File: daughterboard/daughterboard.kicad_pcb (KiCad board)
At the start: 2 copper layers, 85 x 56 mm, 1 part, among them P1 CONN_13X2

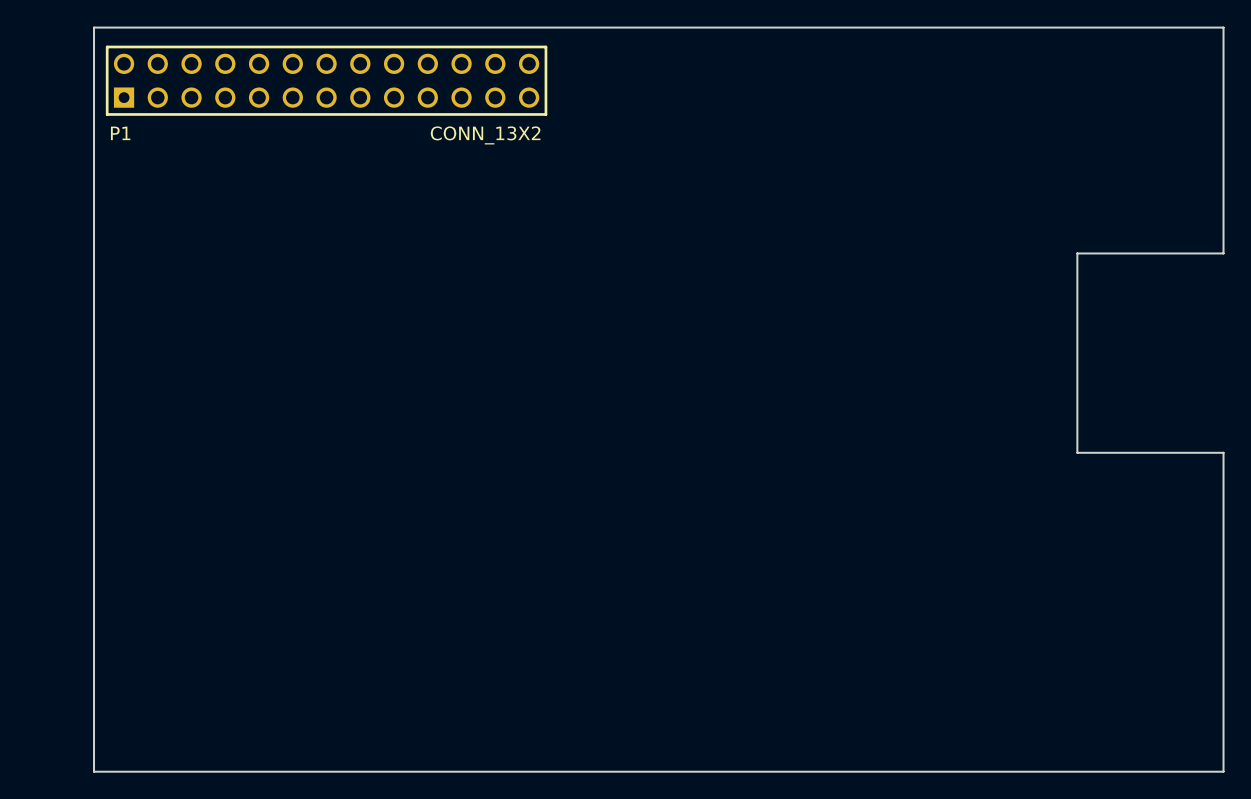
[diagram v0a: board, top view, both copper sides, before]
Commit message: Layout parts (backwards)
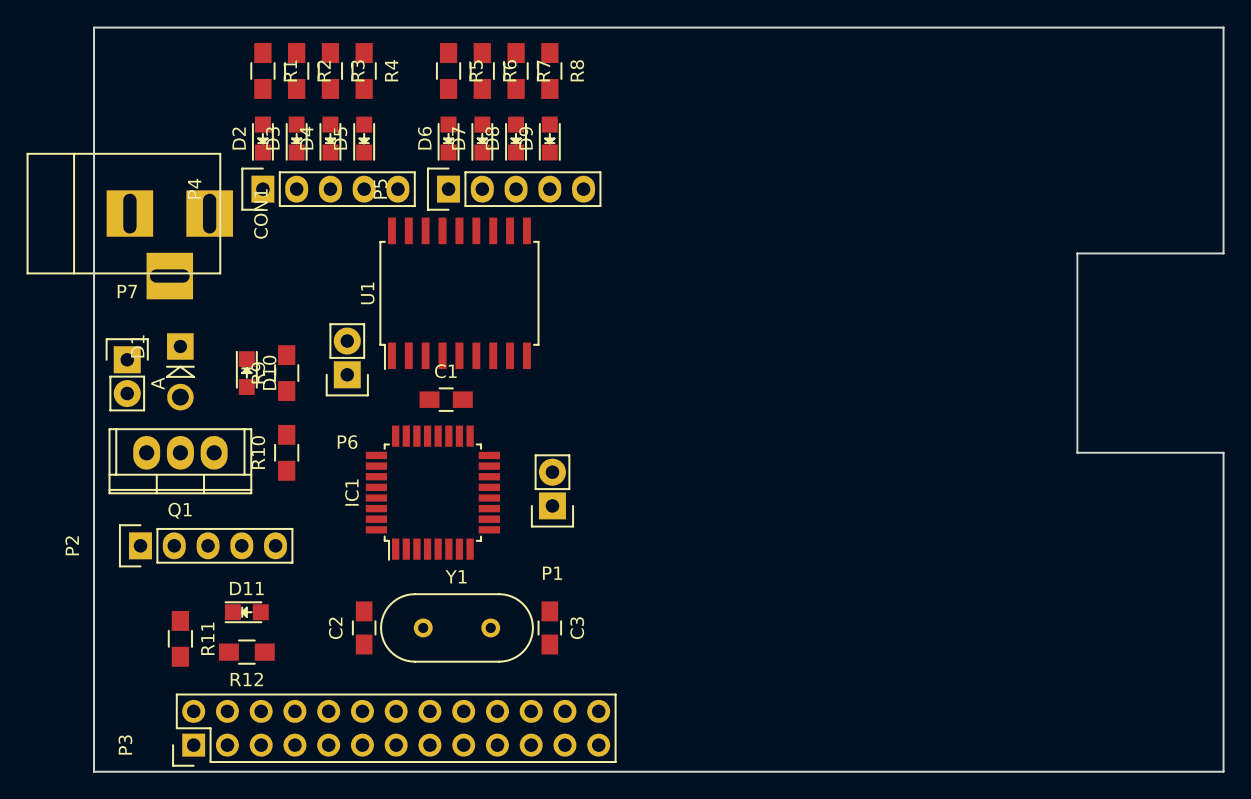
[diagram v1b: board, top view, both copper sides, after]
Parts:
- added C1: 100nF, Capacitors_SMD:C_0805_HandSoldering, F.Cu at (170.0, 153.0)
- added C2: 22pF, Capacitors_SMD:C_0805_HandSoldering, F.Cu at (163.8, 170.2)
- added C3: 22pF, Capacitors_SMD:C_0805_HandSoldering, F.Cu at (177.8, 170.2)
- added CON1: 12V_JACK, Connect:BARREL_JACK, F.Cu at (146.0, 139.0)
- added D1: 1N4007, Diodes_ThroughHole:Diode_DO-41_SOD81_Vertical_AnodeUp, F.Cu at (150.0, 149.0)
- added D10: YELLOW, LEDs:LED_0805, F.Cu at (155.0, 151.0)
- added D11: RED, LEDs:LED_0805, F.Cu at (155.0, 169.0)
- added D2: , LEDs:LED_0805, F.Cu at (156.2, 133.3)
- added D3: , LEDs:LED_0805, F.Cu at (158.8, 133.3)
- added D4: , LEDs:LED_0805, F.Cu at (161.3, 133.3)
- added D5: , LEDs:LED_0805, F.Cu at (163.8, 133.3)
- added D6: , LEDs:LED_0805, F.Cu at (170.2, 133.3)
- added D7: , LEDs:LED_0805, F.Cu at (172.7, 133.3)
- added D8: , LEDs:LED_0805, F.Cu at (175.3, 133.3)
- added D9: , LEDs:LED_0805, F.Cu at (177.8, 133.3)
- added IC1: ATMEGA328P-A, Housings_QFP:TQFP-32_7x7mm_Pitch0.8mm, F.Cu at (169.0, 160.0)
- added P2: EXTRA_PC12345, Pin_Headers:Pin_Header_Straight_1x05, F.Cu at (147.0, 164.0)
- added P3: CONN_13X2, Pin_Headers:Pin_Header_Straight_2x13, F.Cu at (151.0, 179.0)
- added P4: AZIMUTH, Pin_Headers:Pin_Header_Straight_1x05, F.Cu at (156.2, 137.2)
- added P5: ELEVATION, Pin_Headers:Pin_Header_Straight_1x05, F.Cu at (170.2, 137.2)
- added P6: EXTRA_ADC67, Pin_Headers:Pin_Header_Straight_1x02, F.Cu at (162.6, 151.1)
- added P7: VALVE, Pin_Headers:Pin_Header_Straight_1x02, F.Cu at (146.0, 150.0)
- added Q1: TIP120, Power_Integrations:TO-220, F.Cu at (150.0, 157.0)
- added R1: 500, Resistors_SMD:R_0805_HandSoldering, F.Cu at (156.2, 128.3)
- added R10: 1K, Resistors_SMD:R_0805_HandSoldering, F.Cu at (158.0, 157.0)
- added R11: 10K, Resistors_SMD:R_0805_HandSoldering, F.Cu at (150.0, 171.0)
- added R12: 100, Resistors_SMD:R_0805_HandSoldering, F.Cu at (155.0, 172.0)
- added R2: 500, Resistors_SMD:R_0805_HandSoldering, F.Cu at (158.8, 128.3)
- added R3: 500, Resistors_SMD:R_0805_HandSoldering, F.Cu at (161.3, 128.3)
- added R4: 500, Resistors_SMD:R_0805_HandSoldering, F.Cu at (163.8, 128.3)
- added R5: 500, Resistors_SMD:R_0805_HandSoldering, F.Cu at (170.2, 128.3)
- added R6: 500, Resistors_SMD:R_0805_HandSoldering, F.Cu at (172.7, 128.3)
- added R7: 500, Resistors_SMD:R_0805_HandSoldering, F.Cu at (175.3, 128.3)
- added R8: 500, Resistors_SMD:R_0805_HandSoldering, F.Cu at (177.8, 128.3)
- added R9: 100, Resistors_SMD:R_0805_HandSoldering, F.Cu at (158.0, 151.0)
- added U1: ULN2803A, Housings_SOIC:SOIC-18_7.5x11.6mm_Pitch1.27mm, F.Cu at (171.0, 145.0)
- added Y1: 8MHz, Crystals:HC-49V, F.Cu at (170.8, 170.2)
- P1: value CONN_13X2 -> EXTRA_PB01; footprint pin_array_13x2 -> Pin_Headers:Pin_Header_Straight_1x02
- moved P1 36.2 mm to (178.0, 161.0), turned to 180 degrees
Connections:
- P1 pad 1: +3.3V -> Net-(IC1-Pad12)
- P1 pad 2: +5V -> Net-(IC1-Pad13)
